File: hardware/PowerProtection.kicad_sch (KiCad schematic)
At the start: 18 parts, among them IC2 LM74502DDFR, Q1 PSMN012-100YS, Q2 PSMN012-100YS

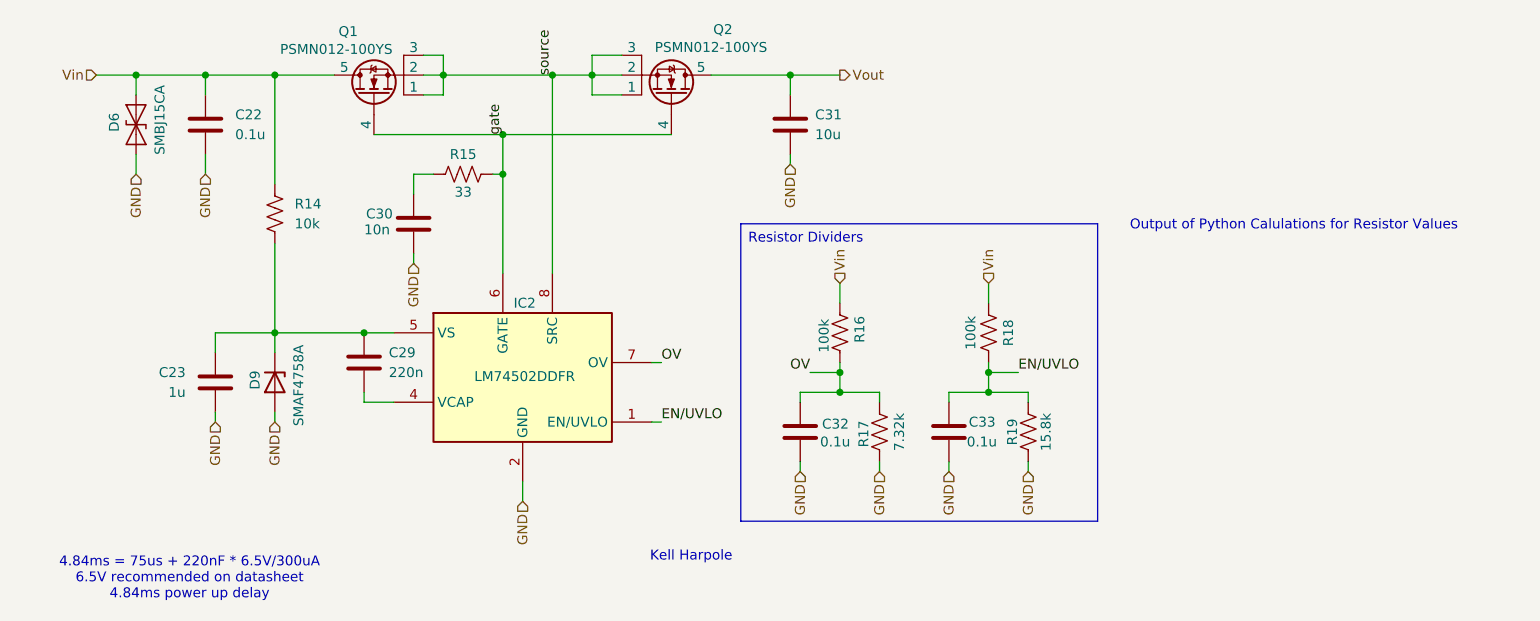
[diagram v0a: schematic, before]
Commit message: Fixed ERC
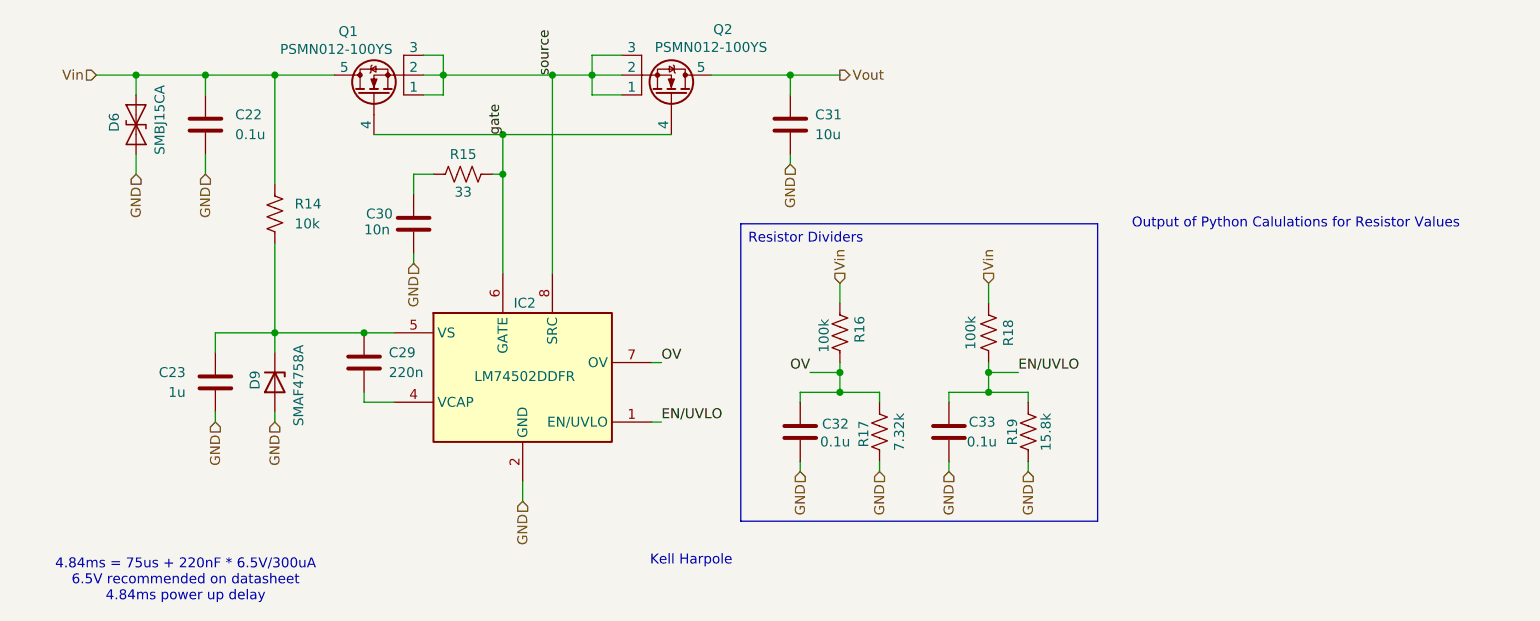
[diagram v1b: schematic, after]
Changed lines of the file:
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@@
 	(text "4.84ms = 75us + 220nF * 6.5V/300uA\n6.5V recommended on datasheet\n4.84ms power up delay"
 		(exclude_from_sim no)
-		(at 32.258 108.966 0)
+		(at 31.75 109.22 0)
 		(effects
 			(font
@@
 	(text "Output of Python Calulations for Resistor Values"
 		(exclude_from_sim no)
-		(at 173.736 63.754 0)
+		(at 173.99 63.5 0)
 		(effects
 			(font
@@
 	(text "Kell Harpole"
 		(exclude_from_sim no)
-		(at 96.52 106.172 0)
+		(at 96.52 106.68 0)
 		(effects
 			(font

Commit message: errors fixed
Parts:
- renumbered C22 to C49, C23 to C50, C29 to C51, C30 to C52, C31 to C53, C32 to C57, C33 to C58, D6 to D12, D9 to D15, IC2 to IC3, Q1 to Q3, Q2 to Q4, R14 to R35, R15 to R36, R16 to R49, R17 to R51, R18 to R53, R19 to R55
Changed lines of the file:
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@@
 		(in_pos_files yes)
 		(dnp no)
-		(property "Reference" "D9"
+		(property "Reference" "D15"
 			(at 40.64 82.296 0)
 			(show_name no)
@@
 			)
 			(project "StrainGaugeBoard"
-				(path "/fb459b39-605b-4b65-b2c9-e248812f4f03/44e29d2e-3b3f-46c8-a788-66edd0238f0d"
-					(reference "D9")
+				(path "/fb459b39-605b-4b65-b2c9-e248812f4f03/ba218eff-eed7-4f95-a304-2420dfea8196"
+					(reference "D15")
 					(unit 1)
 				)
@@
 		(dnp no)
 		(fields_autoplaced yes)
-		(property "Reference" "C29"
+		(property "Reference" "C51"
 			(at 57.785 80.0099 0)
 			(show_name no)
@@
 			)
 			(project "StrainGaugeBoard"
-				(path "/fb459b39-605b-4b65-b2c9-e248812f4f03/44e29d2e-3b3f-46c8-a788-66edd0238f0d"
-					(reference "C29")
+				(path "/fb459b39-605b-4b65-b2c9-e248812f4f03/ba218eff-eed7-4f95-a304-2420dfea8196"
+					(reference "C51")
 					(unit 1)
 				)
@@
 		(in_pos_files yes)
 		(dnp no)
-		(property "Reference" "D6"
+		(property "Reference" "D12"
 			(at 22.606 49.276 0)
 			(show_name no)
@@
 			)
 			(project "StrainGaugeBoard"
-				(path "/fb459b39-605b-4b65-b2c9-e248812f4f03/44e29d2e-3b3f-46c8-a788-66edd0238f0d"
-					(reference "D6")
+				(path "/fb459b39-605b-4b65-b2c9-e248812f4f03/ba218eff-eed7-4f95-a304-2420dfea8196"
+					(reference "D12")
 					(unit 1)
 				)
@@
 		(dnp no)
 		(fields_autoplaced yes)
-		(property "Reference" "R14"
+		(property "Reference" "R35"
 			(at 45.72 60.9599 0)
 			(show_name no)
@@
 			)
 			(project "StrainGaugeBoard"
-				(path "/fb459b39-605b-4b65-b2c9-e248812f4f03/44e29d2e-3b3f-46c8-a788-66edd0238f0d"
-					(reference "R14")
+				(path "/fb459b39-605b-4b65-b2c9-e248812f4f03/ba218eff-eed7-4f95-a304-2420dfea8196"
+					(reference "R35")
 					(unit 1)
 				)
@@
 		(in_pos_files yes)
 		(dnp no)
-		(property "Reference" "R19"
+		(property "Reference" "R55"
 			(at 137.668 90.17 90)
 			(show_name no)
@@
 			)
 			(project "StrainGaugeBoard"
-				(path "/fb459b39-605b-4b65-b2c9-e248812f4f03/44e29d2e-3b3f-46c8-a788-66edd0238f0d"
-					(reference "R19")
+				(path "/fb459b39-605b-4b65-b2c9-e248812f4f03/ba218eff-eed7-4f95-a304-2420dfea8196"
+					(reference "R55")
 					(unit 1)
 				)
@@
 		(in_pos_files yes)
 		(dnp no)
-		(property "Reference" "C22"
+		(property "Reference" "C49"
 			(at 38.1 49.5299 0)
 			(show_name no)
@@
 			)
 			(project "StrainGaugeBoard"
-				(path "/fb459b39-605b-4b65-b2c9-e248812f4f03/44e29d2e-3b3f-46c8-a788-66edd0238f0d"
-					(reference "C22")
+				(path "/fb459b39-605b-4b65-b2c9-e248812f4f03/ba218eff-eed7-4f95-a304-2420dfea8196"
+					(reference "C49")
 					(unit 1)
 				)
@@
 		(in_pos_files yes)
 		(dnp no)
-		(property "Reference" "R15"
+		(property "Reference" "R36"
 			(at 67.31 54.61 90)
 			(show_name no)
@@
 			)
 			(project "StrainGaugeBoard"
-				(path "/fb459b39-605b-4b65-b2c9-e248812f4f03/44e29d2e-3b3f-46c8-a788-66edd0238f0d"
-					(reference "R15")
+				(path "/fb459b39-605b-4b65-b2c9-e248812f4f03/ba218eff-eed7-4f95-a304-2420dfea8196"
+					(reference "R36")
 					(unit 1)
 				)
@@
 		(in_pos_files yes)
 		(dnp no)
-		(property "Reference" "IC2"
+		(property "Reference" "IC3"
 			(at 75.184 73.66 0)
 			(show_name no)
@@
 			)
 			(project "StrainGaugeBoard"
-				(path "/fb459b39-605b-4b65-b2c9-e248812f4f03/44e29d2e-3b3f-46c8-a788-66edd0238f0d"
-					(reference "IC2")
+				(path "/fb459b39-605b-4b65-b2c9-e248812f4f03/ba218eff-eed7-4f95-a304-2420dfea8196"
+					(reference "IC3")
 					(unit 1)
 				)
@@
 		(in_pos_files yes)
 		(dnp no)
-		(property "Reference" "Q1"
+		(property "Reference" "Q3"
 			(at 52.578 38.862 90)
 			(show_name no)
@@
 			)
 			(project "StrainGaugeBoard"
-				(path "/fb459b39-605b-4b65-b2c9-e248812f4f03/44e29d2e-3b3f-46c8-a788-66edd0238f0d"
-					(reference "Q1")
+				(path "/fb459b39-605b-4b65-b2c9-e248812f4f03/ba218eff-eed7-4f95-a304-2420dfea8196"
+					(reference "Q3")
 					(unit 1)
 				)
@@
 		(in_pos_files yes)
 		(dnp no)
-		(property "Reference" "C32"
+		(property "Reference" "C57"
 			(at 113.284 89.154 0)
 			(show_name no)
@@
 			)
 			(project "StrainGaugeBoard"
-				(path "/fb459b39-605b-4b65-b2c9-e248812f4f03/44e29d2e-3b3f-46c8-a788-66edd0238f0d"
-					(reference "C32")
+				(path "/fb459b39-605b-4b65-b2c9-e248812f4f03/ba218eff-eed7-4f95-a304-2420dfea8196"
+					(reference "C57")
 					(unit 1)
 				)
@@
 		(in_pos_files yes)
 		(dnp no)
-		(property "Reference" "C30"
+		(property "Reference" "C52"
 			(at 54.864 62.23 0)
 			(show_name no)
@@
 			)
 			(project "StrainGaugeBoard"
-				(path "/fb459b39-605b-4b65-b2c9-e248812f4f03/44e29d2e-3b3f-46c8-a788-66edd0238f0d"
-					(reference "C30")
+				(path "/fb459b39-605b-4b65-b2c9-e248812f4f03/ba218eff-eed7-4f95-a304-2420dfea8196"
+					(reference "C52")
 					(unit 1)
 				)
@@
 		(in_pos_files yes)
 		(dnp no)
-		(property "Reference" "C31"
+		(property "Reference" "C53"
 			(at 112.395 49.5299 0)
 			(show_name no)
@@
 			)
 			(project "StrainGaugeBoard"
-				(path "/fb459b39-605b-4b65-b2c9-e248812f4f03/44e29d2e-3b3f-46c8-a788-66edd0238f0d"
-					(reference "C31")
+				(path "/fb459b39-605b-4b65-b2c9-e248812f4f03/ba218eff-eed7-4f95-a304-2420dfea8196"
+					(reference "C53")
 					(unit 1)
 				)
@@
 		(in_pos_files yes)
 		(dnp no)
-		(property "Reference" "Q2"
+		(property "Reference" "Q4"
 			(at 100.584 38.608 90)
 			(show_name no)
@@
 			)
 			(project "StrainGaugeBoard"
-				(path "/fb459b39-605b-4b65-b2c9-e248812f4f03/44e29d2e-3b3f-46c8-a788-66edd0238f0d"
-					(reference "Q2")
+				(path "/fb459b39-605b-4b65-b2c9-e248812f4f03/ba218eff-eed7-4f95-a304-2420dfea8196"
+					(reference "Q4")
 					(unit 1)
 				)
@@
 		(in_pos_files yes)
 		(dnp no)
-		(property "Reference" "R17"
+		(property "Reference" "R51"
 			(at 118.618 90.424 90)
 			(show_name no)
@@
 			)
 			(project "StrainGaugeBoard"
-				(path "/fb459b39-605b-4b65-b2c9-e248812f4f03/44e29d2e-3b3f-46c8-a788-66edd0238f0d"
-					(reference "R17")
+				(path "/fb459b39-605b-4b65-b2c9-e248812f4f03/ba218eff-eed7-4f95-a304-2420dfea8196"
+					(reference "R51")
 					(unit 1)
 				)
@@
 		(in_pos_files yes)
 		(dnp no)
-		(property "Reference" "C23"
+		(property "Reference" "C50"
 			(at 31.75 82.5499 0)
 			(show_name no)
@@
 			)
 			(project "StrainGaugeBoard"
-				(path "/fb459b39-605b-4b65-b2c9-e248812f4f03/44e29d2e-3b3f-46c8-a788-66edd0238f0d"
-					(reference "C23")
+				(path "/fb459b39-605b-4b65-b2c9-e248812f4f03/ba218eff-eed7-4f95-a304-2420dfea8196"
+					(reference "C50")
 					(unit 1)
 				)
@@
 		(in_pos_files yes)
 		(dnp no)
-		(property "Reference" "C33"
+		(property "Reference" "C58"
 			(at 132.08 88.9 0)
 			(show_name no)
@@
 			)
 			(project "StrainGaugeBoard"
-				(path "/fb459b39-605b-4b65-b2c9-e248812f4f03/44e29d2e-3b3f-46c8-a788-66edd0238f0d"
-					(reference "C33")
+				(path "/fb459b39-605b-4b65-b2c9-e248812f4f03/ba218eff-eed7-4f95-a304-2420dfea8196"
+					(reference "C58")
 					(unit 1)
 				)
@@
 		(in_pos_files yes)
 		(dnp no)
-		(property "Reference" "R16"
+		(property "Reference" "R49"
 			(at 118.11 78.74 90)
 			(show_name no)
@@
 			)
 			(project "StrainGaugeBoard"
-				(path "/fb459b39-605b-4b65-b2c9-e248812f4f03/44e29d2e-3b3f-46c8-a788-66edd0238f0d"
-					(reference "R16")
+				(path "/fb459b39-605b-4b65-b2c9-e248812f4f03/ba218eff-eed7-4f95-a304-2420dfea8196"
+					(reference "R49")
 					(unit 1)
 				)
@@
 		(in_pos_files yes)
 		(dnp no)
-		(property "Reference" "R18"
+		(property "Reference" "R53"
 			(at 137.16 77.47 90)
 			(show_name no)
@@
 			)
 			(project "StrainGaugeBoard"
-				(path "/fb459b39-605b-4b65-b2c9-e248812f4f03/44e29d2e-3b3f-46c8-a788-66edd0238f0d"
-					(reference "R18")
-					(unit 1)
-				)
+				(path "/fb459b39-605b-4b65-b2c9-e248812f4f03/ba218eff-eed7-4f95-a304-2420dfea8196"
+					(reference "R53")
+					(unit 1)
+				)

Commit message: whoops forgot to push
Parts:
- C52: symbol ECE319H:C -> Device:C
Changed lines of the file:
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@@
 	)
 	(symbol
-		(lib_id "ECE319H:C")
+		(lib_id "Device:C")
 		(at 60.96 63.5 0)
 		(unit 1)
